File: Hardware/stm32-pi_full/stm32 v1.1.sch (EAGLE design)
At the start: 286 parts, among them IC2 AD8519KS, J1 JUMPER-SMT_2_NC_TRACE_NO-SILK, Q1 PNP, Q2 NPN, Q3 NPN, U1 ESP32-WROOM-32D

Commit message: modified:   Hardware/stm32-pi_full/stm32 v1.1 working BoM/JLCSMT_Sample_BOM1.xlsx 	modified:   Hardware/stm32-pi_full/stm32 v1.1.brd 	modified:   Hardware/stm32-pi_full/stm32 v1.1.sch 	modified:   Software/Sombrero_VE_Working6/Src/main.c
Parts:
- S1: MPN (none) -> CST06S08H
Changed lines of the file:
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@@
 <part name="C32" library="rcl" library_urn="urn:adsk.eagle:library:334" deviceset="C-EU" device="C0603" package3d_urn="urn:adsk.eagle:package:23616/2" value="10pF"/>
 <part name="SUPPLY27" library="supply2" library_urn="urn:adsk.eagle:library:372" deviceset="DGND" device=""/>
-<part name="S1" library="switch-omron" library_urn="urn:adsk.eagle:library:377" deviceset="31-XX" device="" package3d_urn="urn:adsk.eagle:package:27487/1"/>
+<part name="S1" library="switch-omron" library_urn="urn:adsk.eagle:library:377" deviceset="31-XX" device="" package3d_urn="urn:adsk.eagle:package:27487/1">
+<attribute name="MPN" value="CST06S08H"/>
+</part>
 <part name="C33" library="rcl" library_urn="urn:adsk.eagle:library:334" deviceset="C-EU" device="C0805" package3d_urn="urn:adsk.eagle:package:23617/2" value="22uF"/>
 <part name="SJ14" library="SparkFun-Jumpers" library_urn="urn:adsk.eagle:library:528" deviceset="JUMPER-SMT_2_NC_TRACE" device="_NO-SILK" package3d_urn="urn:adsk.eagle:package:39286/1"/>

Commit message: MPNs updated
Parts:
- VT1: MPN ADC-028-1-T -> FC68148S
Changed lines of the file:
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@@
 <drawing>
 <settings>
-<setting alwaysvectorfont="no"/>
+<setting alwaysvectorfont="yes"/>
 <setting keepoldvectorfont="yes"/>
 <setting verticaltext="up"/>
@@
 </part>
 <part name="VT1" library="adafruit" library_urn="urn:adsk.eagle:library:420" deviceset="2.1MMJACK" device="SMT" package3d_urn="urn:adsk.eagle:package:6240730/1" value="ADC-028-2-T">
-<attribute name="MPN" value="ADC-028-1-T"/>
+<attribute name="MPN" value="FC68148S"/>
 </part>
 <part name="RJ1" library="95501-6889 rj45 smt" deviceset="95501-6889" device="" value="95501-6889"/>

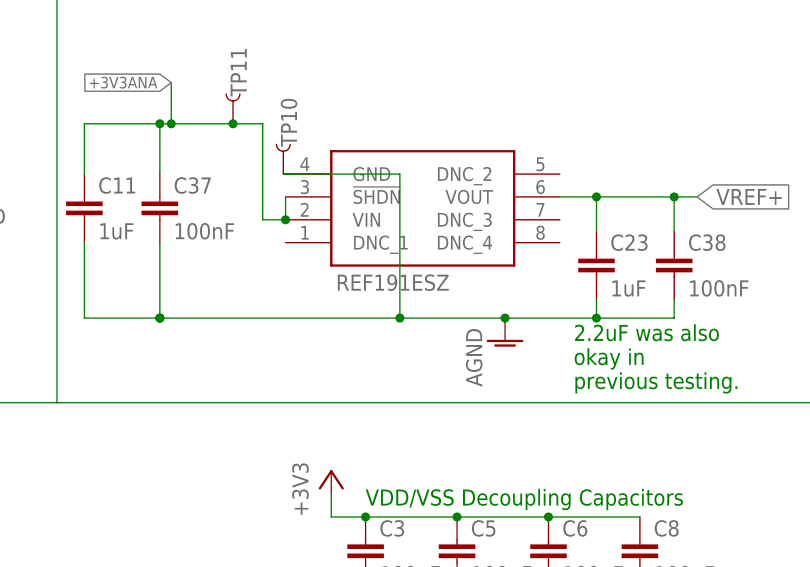
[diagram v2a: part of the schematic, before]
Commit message: MPNs updated
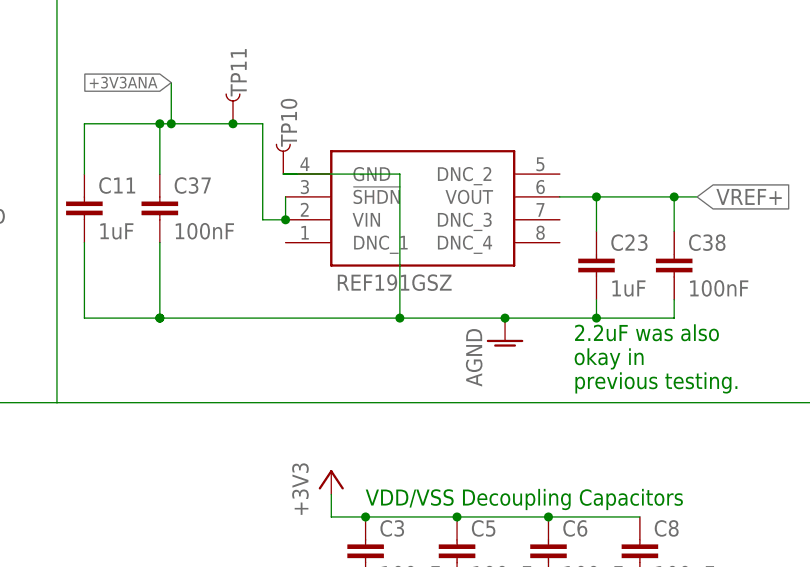
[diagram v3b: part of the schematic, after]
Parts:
- REF19X: MPN REF191ESZ -> REF191GSZ
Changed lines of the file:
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@@
 <part name="SJ14" library="SparkFun-Jumpers" library_urn="urn:adsk.eagle:library:528" deviceset="JUMPER-SMT_2_NC_TRACE" device="_NO-SILK" package3d_urn="urn:adsk.eagle:package:39286/1"/>
 <part name="REF19X" library="LT1461AIS8" deviceset="LT1461AIS8-3.3#PBF" device="" value="REF191ESZ">
-<attribute name="MPN" value="REF191ESZ"/>
+<attribute name="MPN" value="REF191GSZ"/>
 </part>
 <part name="C23" library="rcl" library_urn="urn:adsk.eagle:library:334" deviceset="C-EU" device="C0603" package3d_urn="urn:adsk.eagle:package:23616/2" value="1uF"/>
